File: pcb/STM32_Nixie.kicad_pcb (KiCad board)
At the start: 2 copper layers, 15 parts, among them U1 IC_HV5622PG-G, U2 IC_HV5622PG-G, U3 STM32F100C4Tx

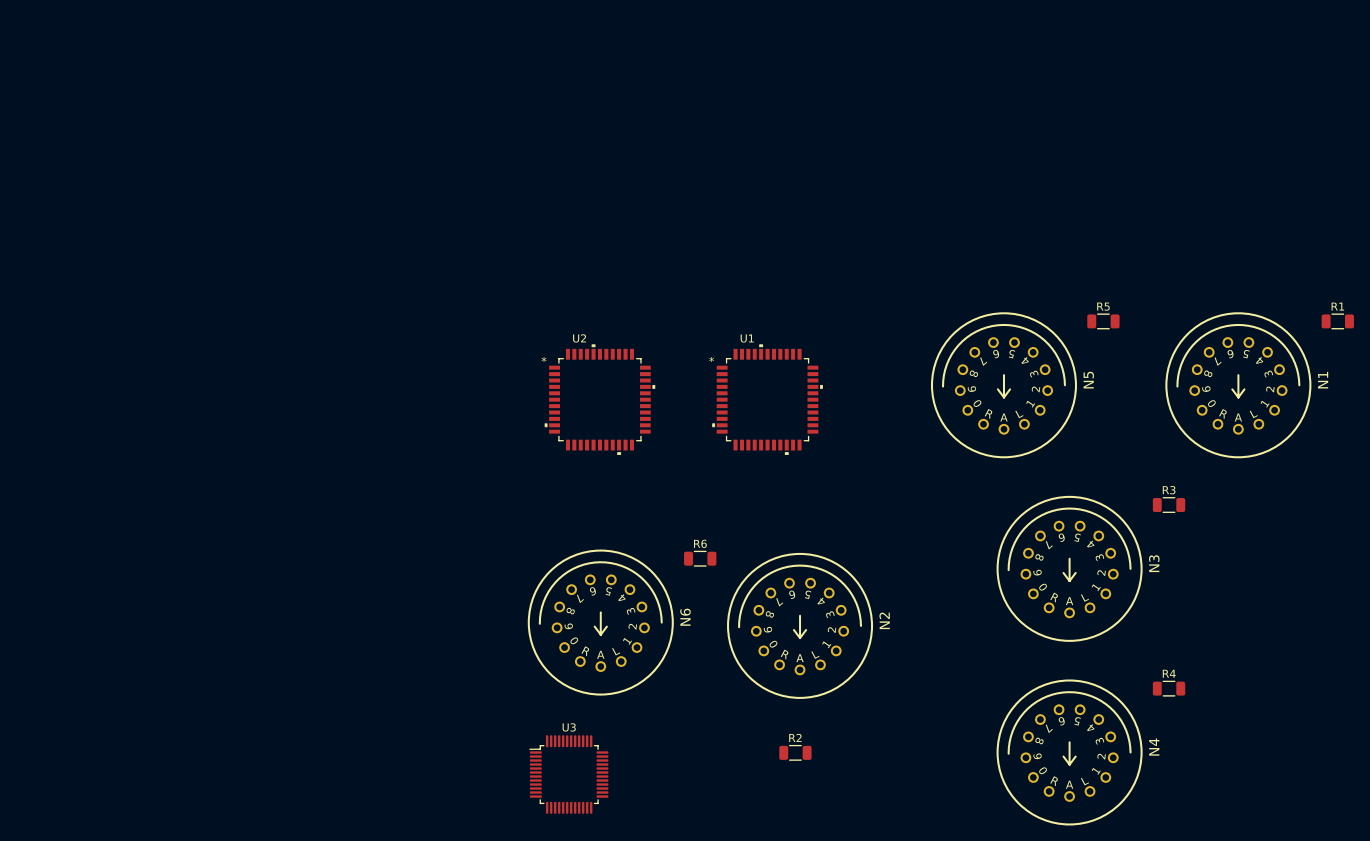
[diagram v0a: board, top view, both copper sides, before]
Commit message: Added ferrite to ADC input, Coin-Cell, and STLINK conn.
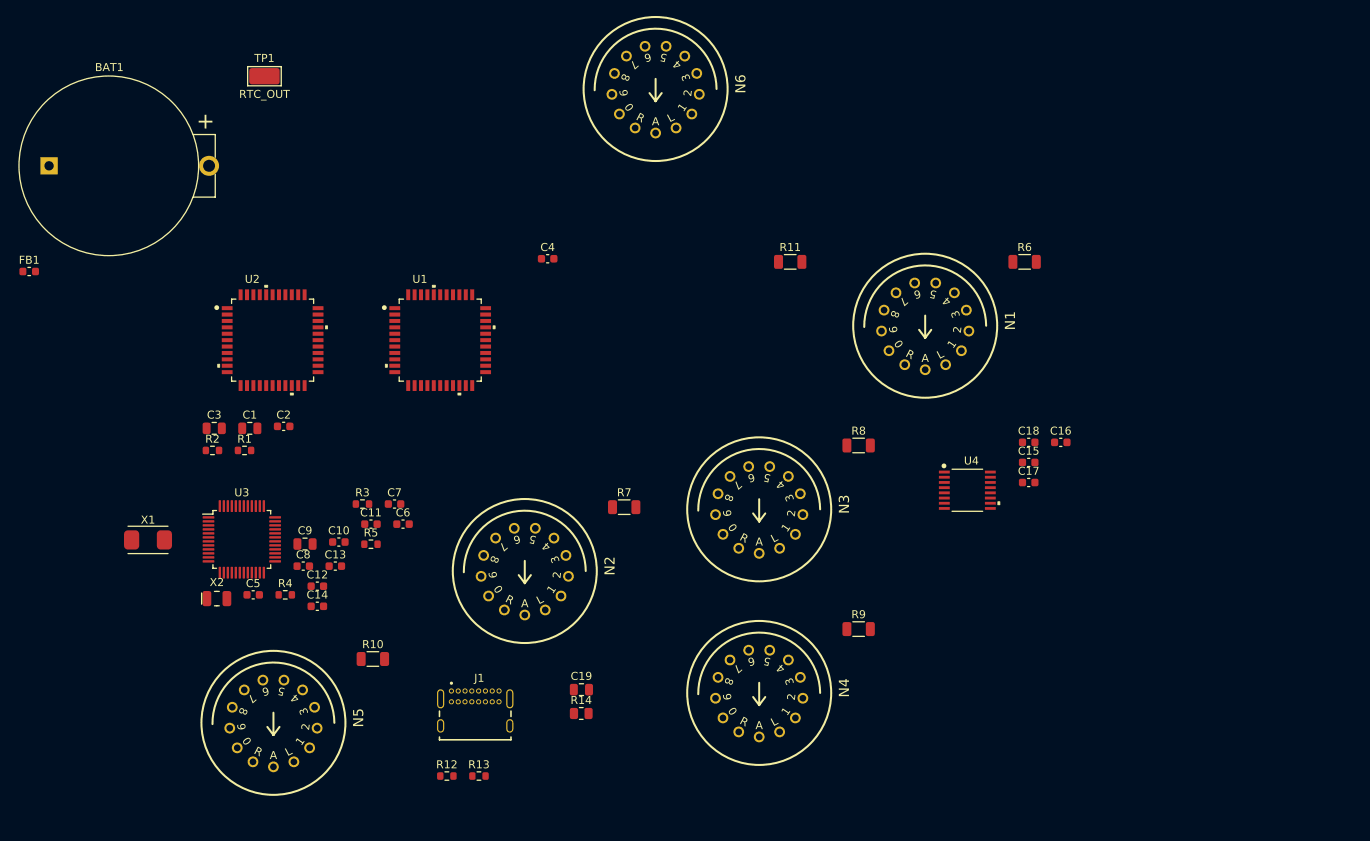
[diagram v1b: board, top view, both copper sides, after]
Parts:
- added BAT1: BS-7, arjun_footprints:Battery_Holder_Coin_2032_BS-7, F.Cu at (110.9, 55.8)
- added C1: CAP_CER_4u7_50V_X5R_0805, Capacitor_SMD:C_0805_2012Metric, F.Cu at (136.0, 88.6)
- added C10: CAP_CER_0u1_50V_X7R_0603, Capacitor_SMD:C_0603_1608Metric, F.Cu at (147.1, 102.8)
- added C11: CAP_CER_0u1_50V_X7R_0603, Capacitor_SMD:C_0603_1608Metric, F.Cu at (151.1, 100.6)
- added C12: CAP_CER_0u1_50V_X7R_0603, Capacitor_SMD:C_0603_1608Metric, F.Cu at (144.4, 108.3)
- added C13: CAP_CER_1u_25V_X5R_0603, Capacitor_SMD:C_0603_1608Metric, F.Cu at (146.7, 105.8)
- added C14: CAP_CER_0u1_50V_X7R_0603, Capacitor_SMD:C_0603_1608Metric, F.Cu at (144.4, 110.8)
- added C15: CAP_CER_1u_25V_X5R_0603, Capacitor_SMD:C_0603_1608Metric, F.Cu at (233.3, 92.9)
- added C16: CAP_CER_0u1_50V_X7R_0603, Capacitor_SMD:C_0603_1608Metric, F.Cu at (237.3, 90.3)
- added C17: CAP_CER_0u1_50V_X7R_0603, Capacitor_SMD:C_0603_1608Metric, F.Cu at (233.3, 95.4)
- added C18: CAP_CER_1u_25V_X5R_0603, Capacitor_SMD:C_0603_1608Metric, F.Cu at (233.3, 90.3)
- added C19: CAP_CER_4700p_250V_X7R_0805, Capacitor_SMD:C_0805_2012Metric, F.Cu at (177.4, 121.3)
- added C2: CAP_CER_0u1_50V_X7R_0603, Capacitor_SMD:C_0603_1608Metric, F.Cu at (140.2, 88.3)
- added C3: CAP_CER_4u7_50V_X5R_0805, Capacitor_SMD:C_0805_2012Metric, F.Cu at (131.5, 88.6)
- added C4: CAP_CER_0u1_50V_X7R_0603, Capacitor_SMD:C_0603_1608Metric, F.Cu at (173.2, 67.4)
- added C5: CAP_CER_27p_50V_NP0_0603, Capacitor_SMD:C_0603_1608Metric, F.Cu at (136.4, 109.4)
- added C6: CAP_CER_27p_50V_NP0_0603, Capacitor_SMD:C_0603_1608Metric, F.Cu at (155.1, 100.6)
- added C7: CAP_CER_8p_50V_NP0_0603, Capacitor_SMD:C_0603_1608Metric, F.Cu at (154.1, 98.1)
- added C8: CAP_CER_8p_50V_NP0_0603, Capacitor_SMD:C_0603_1608Metric, F.Cu at (142.6, 105.8)
- added C9: CAP_CER_10u_16V_X5R_0805, Capacitor_SMD:C_0805_2012Metric, F.Cu at (142.9, 103.1)
- added FB1: FER_1K_600mA_0603, Inductor_SMD:L_0603_1608Metric, F.Cu at (108.4, 69.0)
- added J1: CONN_USBC_RCPT_USB2.0_USB4085-GF-A, arjun_footprints:GCT_USB4085-GF-A_REVA4, F.Cu at (164.1, 125.8)
- added R10: RES_17K4_1P_1/4W_1206, Resistor_SMD:R_1206_3216Metric, F.Cu at (151.3, 117.4)
- added R11: RES_17K4_1P_1/4W_1206, Resistor_SMD:R_1206_3216Metric, F.Cu at (203.5, 67.8)
- added R12: RES_5K11_1P_1/10W_0603, Resistor_SMD:R_0603_1608Metric, F.Cu at (160.6, 132.1)
- added R13: RES_5K11_1P_1/10W_0603, Resistor_SMD:R_0603_1608Metric, F.Cu at (164.6, 132.1)
- added R14: RES_0R_1/8W_0805, Resistor_SMD:R_0805_2012Metric, F.Cu at (177.4, 124.2)
- added R7: RES_17K4_1P_1/4W_1206, Resistor_SMD:R_1206_3216Metric, F.Cu at (182.8, 98.4)
- added R8: RES_17K4_1P_1/4W_1206, Resistor_SMD:R_1206_3216Metric, F.Cu at (212.1, 90.7)
- added R9: RES_17K4_1P_1/4W_1206, Resistor_SMD:R_1206_3216Metric, F.Cu at (212.1, 113.7)
- added TP1: RTC_OUT, arjun_footprints:TestPoint_Keystone_5019_Minature, F.Cu at (137.8, 44.6)
- added U4: IC_LVL_MC14504BDTR2G, arjun_footprints:MC14504BDTR2G, F.Cu at (225.7, 96.3)
- added X1: XTAL_8M_20PPM_18pF_ECS-80-18-30-JGN-TR, arjun_footprints:SMD-2_5x3.2mm_ECS, F.Cu at (123.2, 102.5)
- added X2: XTAL_32K768_10PPM_7pF_ECS-.327-7-34B-C-TR, arjun_footprints:SMD-2_3.2x1.5mm_ECS, F.Cu at (131.8, 109.9)
- R1, R2, R3: value R_17K4_1P_1/4W_1206 -> RES_10K_1P_1/10W_0603; footprint Resistor_SMD:R_1206_3216Metric -> Resistor_SMD:R_0603_1608Metric
- R4: value R_17K4_1P_1/4W_1206 -> RES_732R_1P_1/10W_0603; footprint Resistor_SMD:R_1206_3216Metric -> Resistor_SMD:R_0603_1608Metric
- R5: value R_17K4_1P_1/4W_1206 -> RES_0R_1/10W_0603; footprint Resistor_SMD:R_1206_3216Metric -> Resistor_SMD:R_0603_1608Metric
- R6: value R_17K4_1P_1/4W_1206 -> RES_17K4_1P_1/4W_1206
- U3: value STM32F100C4Tx -> IC_MCU_STM32F100C4T6B_48LQFP
- moved R1 137.6 mm to (135.3, 91.4)
- moved R4 111.1 mm to (140.4, 109.4)
- moved R3 100.8 mm to (150.0, 98.1)
- moved N5 100.6 mm to (138.9, 125.4)
- moved R5 95.7 mm to (151.1, 103.1)
- moved R2 82.1 mm to (131.3, 91.4)
- moved N6 67.0 mm to (186.7, 46.2)
- moved R6 55.0 mm to (232.8, 67.8)
- moved U3 50.4 mm to (135.0, 102.5)
- moved U1 41.6 mm to (159.8, 77.6)
- moved U2 41.6 mm to (138.8, 77.6)
- moved N1 39.9 mm to (220.4, 75.8)
- moved N3 39.5 mm to (199.6, 98.7)
- moved N4 39.5 mm to (199.6, 121.7)
- moved N2 35.1 mm to (170.3, 106.4)
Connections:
- R1 pad 1: 180V -> +12V
- R1 pad 2: /Shift Registers/H1/NIXIE_A -> /Shift Registers/nPOL_12V
- R2 pad 1: 180V -> /PWM_nBL_12V
- R2 pad 2: /Shift Registers/H2/NIXIE_A -> GND
- R3 pad 1: 180V -> +3.3V
- R3 pad 2: /Shift Registers/M1/NIXIE_A -> /MCU/nRST
- R4 pad 1: 180V -> /MCU/OSC_OUT
- R4 pad 2: /Shift Registers/M2/NIXIE_A -> /MCU/OSC_OUT_R
- R5 pad 1: 180V -> /MCU/OSC32_OUT
- R5 pad 2: /Shift Registers/S1/NIXIE_A -> /MCU/OSC32_OUT_R
- R6 pad 2: /Shift Registers/S2/NIXIE_A -> /Shift Registers/H1/NIXIE_A
- U1 pad 23: unconnected-(U1-Pad23) -> /Shift Registers/DATA_CHAIN
- U1 pad 27: unconnected-(U1-Pad27) -> /Shift Registers/nPOL_12V
- U1 pad 28: unconnected-(U1-Pad28) -> /SPI_SCK_12V
- U1 pad 29: unconnected-(U1-Pad29) -> GND
- U1 pad 30: unconnected-(U1-Pad30) -> +12V
- U1 pad 31: unconnected-(U1-Pad31) -> /SPI_nCS_nLE_12V
- U1 pad 32: unconnected-(U1-Pad32) -> /SPI_PICO_12V
- U1 pad 33: unconnected-(U1-Pad33) -> /PWM_nBL_12V
- U2 pad 27: unconnected-(U2-Pad27) -> /PWM_nBL_12V
- U2 pad 28: unconnected-(U2-Pad28) -> /SPI_SCK_12V
- U2 pad 29: unconnected-(U2-Pad29) -> GND
- U2 pad 30: unconnected-(U2-Pad30) -> +12V
- U2 pad 31: unconnected-(U2-Pad31) -> /SPI_nCS_nLE_12V
- U2 pad 32: unconnected-(U2-Pad32) -> /Shift Registers/DATA_CHAIN
- U2 pad 33: unconnected-(U2-Pad33) -> /Shift Registers/nPOL_12V
- U3 pad 1: unconnected-(U3-Pad1) -> 180V
- U3 pad 11: unconnected-(U3-Pad11) -> /MCU/HV_MON_BUF
- U3 pad 12: unconnected-(U3-Pad12) -> /MCU/UART_VCP_TX
- U3 pad 13: unconnected-(U3-Pad13) -> /MCU/UART_VCP_RX
- U3 pad 14: unconnected-(U3-Pad14) -> /SPI_nCS_nLE_3V3
- U3 pad 15: unconnected-(U3-Pad15) -> /SPI_SCK_3V3
- U3 pad 16: unconnected-(U3-Pad16) -> /PWM_nBL_3V3
- U3 pad 17: unconnected-(U3-Pad17) -> /SPI_PICO_3V3
- U3 pad 18: unconnected-(U3-Pad18) -> /nPOL_3V3
- U3 pad 2: unconnected-(U3-Pad2) -> /MCU/RTC_OUT
- U3 pad 23: unconnected-(U3-Pad23) -> GND
- U3 pad 24: unconnected-(U3-Pad24) -> +3.3V
- U3 pad 25: unconnected-(U3-Pad25) -> /MCU/HV_EN
- U3 pad 3: unconnected-(U3-Pad3) -> /MCU/OSC32_IN
- U3 pad 30: unconnected-(U3-Pad30) -> /MCU/UART_BL_TX
- U3 pad 31: unconnected-(U3-Pad31) -> /MCU/UART_BL_RX
- U3 pad 34: unconnected-(U3-Pad34) -> /MCU/SWDIO
- U3 pad 35: unconnected-(U3-Pad35) -> GND
- U3 pad 36: unconnected-(U3-Pad36) -> +3.3V
- U3 pad 37: unconnected-(U3-Pad37) -> /MCU/SWCLK
- U3 pad 39: unconnected-(U3-Pad39) -> /MCU/SWO
- U3 pad 4: unconnected-(U3-Pad4) -> /MCU/OSC32_OUT
- U3 pad 47: unconnected-(U3-Pad47) -> GND
- U3 pad 48: unconnected-(U3-Pad48) -> +3.3V
- U3 pad 5: unconnected-(U3-Pad5) -> /MCU/OSC_IN
- U3 pad 6: unconnected-(U3-Pad6) -> /MCU/OSC_OUT
- U3 pad 7: unconnected-(U3-Pad7) -> /MCU/nRST
- U3 pad 8: unconnected-(U3-Pad8) -> GND
- U3 pad 9: unconnected-(U3-Pad9) -> +3.3VA

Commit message: Added snubber DNP footprints and named nets on power page.
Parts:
- added C10: CAP_CER_0u1_50V_X7R_0603, Capacitor_SMD:C_0603_1608Metric, F.Cu at (92.3, 121.9)
- added C21: CAP_CER_1u_50V_X7R_0805, Capacitor_SMD:C_0805_2012Metric, F.Cu at (16.6, 76.7)
- added C22: CAP_CER_0u1_50V_X7R_0603, Capacitor_SMD:C_0603_1608Metric, F.Cu at (42.1, 128.2)
- added C23: CAP_CER_100u_10V_X5R_1210, Capacitor_SMD:C_1210_3225Metric, F.Cu at (23.4, 132.2)
- added C24: CAP_CER_100u_10V_X5R_1210, Capacitor_SMD:C_1210_3225Metric, F.Cu at (49.3, 111.8)
- added C25: CAP_CER_100u_10V_X5R_1210, Capacitor_SMD:C_1210_3225Metric, F.Cu at (29.0, 132.3)
- added C26: CAP_CER_1u_50V_X7R_0805, Capacitor_SMD:C_0805_2012Metric, F.Cu at (37.9, 128.4)
- added C27: CAP_CER_0u1_50V_X7R_0603, Capacitor_SMD:C_0603_1608Metric, F.Cu at (42.3, 130.7)
- added C28: CAP_CER_0u1_50V_X7R_0603, Capacitor_SMD:C_0603_1608Metric, F.Cu at (49.6, 121.4)
- added C29: CAP_CER_4u7_50V_X7R_1206, Capacitor_SMD:C_1206_3216Metric, F.Cu at (40.4, 118.3)
- added C30: CAP_CER_4u7_50V_X7R_1206, Capacitor_SMD:C_1206_3216Metric, F.Cu at (40.4, 121.7)
- added C31: CAP_CER_0u01_50V_X7R_0603, Capacitor_SMD:C_0603_1608Metric, F.Cu at (47.7, 124.0)
- added C32: CAP_CER_0u1_50V_X7R_0603, Capacitor_SMD:C_0603_1608Metric, F.Cu at (42.3, 133.2)
- added C33: CAP_CER_1u_16V_X7R_0603, Capacitor_SMD:C_0603_1608Metric, F.Cu at (53.7, 121.4)
- added C34: CAP_CER_1500p_50V_NP0_0603, Capacitor_SMD:C_0603_1608Metric, F.Cu at (38.3, 133.7)
- added C35: CAP_CER_3300p_50V_X7R_0603, Capacitor_SMD:C_0603_1608Metric, F.Cu at (46.3, 131.5)
- added C36: CAP_CER_7p_50V_NP0_0603, Capacitor_SMD:C_0603_1608Metric, F.Cu at (46.3, 129.0)
- added C37: CAP_CER_1u_50V_X7R_0805, Capacitor_SMD:C_0805_2012Metric, F.Cu at (45.4, 121.2)
- added C38: CAP_CER_0u1_50V_X7R_0603, Capacitor_SMD:C_0603_1608Metric, F.Cu at (51.7, 126.4)
- added C39: CAP_CER_DNP_0805, Capacitor_SMD:C_0805_2012Metric, F.Cu at (33.2, 83.5)
- added C40: CAP_CER_DNP_0805, Capacitor_SMD:C_0805_2012Metric, F.Cu at (28.3, 83.3)
- added C41: CAP_CER_0u1_50V_X7R_0603, Capacitor_SMD:C_0603_1608Metric, F.Cu at (62.8, 116.0)
- added C42: CAP_CER_1u_50V_X7R_0805, Capacitor_SMD:C_0805_2012Metric, F.Cu at (50.6, 115.7)
- added C43: CAP_CER_0u1_250V_X7R_0805, Capacitor_SMD:C_0805_2012Metric, F.Cu at (34.1, 131.7)
- added C44: CAP_CER_1u_250V_X7R_2220, Capacitor_SMD:C_2220_5650Metric, F.Cu at (33.3, 120.1)
- added C45: CAP_CER_1u_250V_X7R_2220, Capacitor_SMD:C_2220_5650Metric, F.Cu at (24.8, 126.6)
- added C46: CAP_CER_1u_250V_X7R_2220, Capacitor_SMD:C_2220_5650Metric, F.Cu at (33.9, 113.2)
- added C47: CAP_CER_0u1_50V_X7R_0603, Capacitor_SMD:C_0603_1608Metric, F.Cu at (46.5, 143.3)
- added C48: CAP_CER_0u01_50V_X7R_0603, Capacitor_SMD:C_0603_1608Metric, F.Cu at (38.4, 148.3)
- added C49: CAP_CER_0u01_50V_X7R_0603, Capacitor_SMD:C_0603_1608Metric, F.Cu at (38.4, 143.3)
- added C51: CAP_CER_0u01_50V_X7R_0603, Capacitor_SMD:C_0603_1608Metric, F.Cu at (60.6, 154.9)
- added C52: CAP_CER_0u1_50V_X7R_0603, Capacitor_SMD:C_0603_1608Metric, F.Cu at (61.1, 151.9)
- added C53: CAP_CER_4u7_50V_X5R_0805, Capacitor_SMD:C_0805_2012Metric, F.Cu at (56.8, 152.1)
- added C9: CAP_CER_0u1_50V_X7R_0603, Capacitor_SMD:C_0603_1608Metric, F.Cu at (94.0, 119.4)
- added D1: D_300V_2A_SMB, Diode_SMD:D_SMB, F.Cu at (35.6, 88.9)
- added FB1: FER_1K_0A6_0603, Inductor_SMD:L_0603_1608Metric, F.Cu at (88.3, 125.4)
- added FB2: FER_120R_2A_0603, Inductor_SMD:L_0603_1608Metric, F.Cu at (63.3, 111.0)
- added FB3: FER_120R_2A_0603, Inductor_SMD:L_0603_1608Metric, F.Cu at (59.3, 113.5)
- added FB4: FER_120R_2A_0603, Inductor_SMD:L_0603_1608Metric, F.Cu at (58.8, 116.0)
- added FB5: FER_33R_6A_0603, Inductor_SMD:L_0603_1608Metric, F.Cu at (64.6, 154.4)
- added J1: CON_SAMTEC_14P_2R_1m27_P_KEY_FTSH-107-01-L-DV-K-TR, arjun_footprints:CON_FTSH-107-01-x-DV-K, F.Cu at (87.8, 113.9)
- added J2: CONN_USBC_RCPT_USB2.0_USB4085-GF-A, arjun_footprints:GCT_USB4085-GF-A_REVA4, F.Cu at (60.2, 145.6)
- added JP1: SolderJumper_3_Bridged12, Jumper:SolderJumper-3_P1.3mm_Bridged12_RoundedPad1.0x1.5mm_NumberLabels, F.Cu at (85.1, 119.9)
- added L1: IND_22u_1A4_163m8R_4r9x4r9x4, arjun_footprints:IND_Taiyo-Yuden_NR-50xx, F.Cu at (43.2, 104.1)
- added L2: IND_3u3_4A2_35m1R_5x5x4r5, arjun_footprints:IND_VLS5045EX-3R3N, F.Cu at (32.3, 126.9)
- added N1: IN-3, arjun_footprints:IN-3, F.Cu at (86.7, 142.3)
- added N2: IN-3, arjun_footprints:IN-3, F.Cu at (86.7, 134.1)
- added Q1: NFET_250V_10A_TPH1110FNH,L1Q, arjun_footprints:SOP Advance_TOS, F.Cu at (26.4, 89.5)
- added R10: RES_10K_1P_1/10W_0603, Resistor_SMD:R_0603_1608Metric, F.Cu at (88.3, 122.9)
- added R17: RES_10K_1P_1/10W_0603, Resistor_SMD:R_0603_1608Metric, F.Cu at (38.3, 131.2)
- added R18: RES_0R_1/10W_0603, Resistor_SMD:R_0603_1608Metric, F.Cu at (54.8, 115.4)
- added R19: RES_10K_1P_1/10W_0603, Resistor_SMD:R_0603_1608Metric, F.Cu at (63.3, 113.5)
- added R20: RES_10K_1P_1/10W_0603, Resistor_SMD:R_0603_1608Metric, F.Cu at (47.7, 126.5)
- added R23: RES_10K_1P_1/10W_0603, Resistor_SMD:R_0603_1608Metric, F.Cu at (33.8, 134.4)
- added R24: RES_61K9_1P_1/10W_0603, Resistor_SMD:R_0603_1608Metric, F.Cu at (55.7, 123.9)
- added R25: RES_0R_1/10W_0603, Resistor_SMD:R_0603_1608Metric, F.Cu at (58.8, 118.5)
- added R26: RES_0R_1/10W_0603, Resistor_SMD:R_0603_1608Metric, F.Cu at (54.8, 118.4)
- added R27: RES_69K8_1P_1/10W_0603, Resistor_SMD:R_0603_1608Metric, F.Cu at (50.3, 129.0)
- added R28: RES_100R_1P_1/10W_0603, Resistor_SMD:R_0603_1608Metric, F.Cu at (59.3, 111.0)
- added R29: RES_R030_1P_1W_1206, Resistor_SMD:R_1206_3216Metric, F.Cu at (18.3, 87.4)
- added R3: RES_150K_1P_1/4W_1206, Resistor_SMD:R_1206_3216Metric, F.Cu at (94.0, 131.4)
- added R30: RES_DNP_0805, Resistor_SMD:R_0805_2012Metric, F.Cu at (23.9, 83.4)
- added R31: RES_DNP_0805, Resistor_SMD:R_0805_2012Metric, F.Cu at (37.4, 83.5)
- added R32: RES_499K_1P_1/4W_0805, Resistor_SMD:R_0805_2012Metric, F.Cu at (50.5, 118.7)
- added R33: RES_2K8_1P_1/10W_0603, Resistor_SMD:R_0603_1608Metric, F.Cu at (51.7, 123.9)
- added R34: RES_10K_1P_1/10W_0603, Resistor_SMD:R_0603_1608Metric, F.Cu at (42.5, 145.8)
- added R35: RES_10K_1P_1/10W_0603, Resistor_SMD:R_0603_1608Metric, F.Cu at (42.5, 140.8)
- added R36: RES_10K_1P_1/10W_0603, Resistor_SMD:R_0603_1608Metric, F.Cu at (38.4, 145.8)
- added R37: RES_10K_1P_1/10W_0603, Resistor_SMD:R_0603_1608Metric, F.Cu at (42.5, 143.3)
- added R38: RES_10K_1P_1/10W_0603, Resistor_SMD:R_0603_1608Metric, F.Cu at (38.4, 140.8)
- added R39: RES_10K_1P_1/10W_0603, Resistor_SMD:R_0603_1608Metric, F.Cu at (46.5, 140.8)
- added R4: RES_150K_1P_1/4W_1206, Resistor_SMD:R_1206_3216Metric, F.Cu at (94.0, 134.7)
- added R40: RES_0R_1/8W_0805, Resistor_SMD:R_0805_2012Metric, F.Cu at (73.4, 151.4)
- added R41: RES_5K11_1P_1/10W_0603, Resistor_SMD:R_0603_1608Metric, F.Cu at (65.1, 151.9)
- added R42: RES_5K11_1P_1/10W_0603, Resistor_SMD:R_0603_1608Metric, F.Cu at (56.6, 154.9)
- added R5: RES_10K_1P_1/10W_0603, Resistor_SMD:R_0603_1608Metric, F.Cu at (84.3, 125.4)
- added R8: RES_10K_1P_1/10W_0603, Resistor_SMD:R_0603_1608Metric, F.Cu at (84.3, 122.9)
- added R9: RES_10K_1P_1/10W_0603, Resistor_SMD:R_0603_1608Metric, F.Cu at (90.0, 119.4)
- added S1: SW_TACT_PTS645SM43SMTR92_LFS, arjun_footprints:Switch_Tactile_SMD_6x6mm_PTS645, F.Cu at (76.8, 121.0)
- added S2: SW_TACT_PTS645SM43SMTR92_LFS, arjun_footprints:Switch_Tactile_SMD_6x6mm_PTS645, F.Cu at (76.8, 113.5)
- added SW1: ENC_SPST_24PPR_PEC12R-4225F-S0024, arjun_footprints:ENC_SPST_PEC12R-4x25F-Sxxx, F.Cu at (22.8, 148.3)
- added U5: REG_SW_BOOST_TI_TLV61046ADBV, arjun_footprints:SOT-23-6_TI, F.Cu at (45.8, 117.5)
- added U6: REG_SW_BOOST_TI_LM51561HPWPR, arjun_footprints:PWP0014H-MFG, F.Cu at (20.3, 96.5)
- added U7: REG_LDO_3V3_250mA_TI_LP5907MFX-3.3, arjun_footprints:SOT-23-5_TI, F.Cu at (54.7, 111.9)
- added U8: IC_FTDI_FT231XS, Package_SO:SSOP-20_3.9x8.7mm_P0.635mm, F.Cu at (75.2, 144.7)
- U3: footprint Package_QFP:LQFP-48_7x7mm_P0.5mm -> arjun_footprints:LQFP-48_7x7mm_P0.5mm
- renumbered C9 to C11, C10 to C12, C11 to C13, C12 to C14, C13 to C15, C14 to C16, C15 to C17, C16 to C18, C17 to C19, C3 to C2, C18 to C20, C2 to C3, C7 to C6, C6 to C7, N1 to N3, N2 to N4, N3 to N5, N4 to N6, N5 to N7, N6 to N8, R6 to R11, R7 to R12, R8 to R13, R9 to R14, R10 to R15, R11 to R16, R4 to R6, R5 to R7
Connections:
- net /Shift Registers/DATA_CHAIN renamed /Nixie Display/DATA_CHAIN
- net /Shift Registers/H1/NIXIE_A renamed /Nixie Display/H1/NIXIE_A
- net /Shift Registers/H1_0 renamed /Nixie Display/H1_0
- net /Shift Registers/H1_1 renamed /Nixie Display/H1_1
- net /Shift Registers/H1_2 renamed /Nixie Display/H1_2
- net /Shift Registers/H1_3 renamed /Nixie Display/H1_3
- net /Shift Registers/H1_4 renamed /Nixie Display/H1_4
- net /Shift Registers/H1_5 renamed /Nixie Display/H1_5
- net /Shift Registers/H1_6 renamed /Nixie Display/H1_6
- net /Shift Registers/H1_7 renamed /Nixie Display/H1_7
- net /Shift Registers/H1_8 renamed /Nixie Display/H1_8
- net /Shift Registers/H1_9 renamed /Nixie Display/H1_9
- net /Shift Registers/H2/NIXIE_A renamed /Nixie Display/H2/NIXIE_A
- net /Shift Registers/H2_0 renamed /Nixie Display/H2_0
- net /Shift Registers/H2_1 renamed /Nixie Display/H2_1
- net /Shift Registers/H2_2 renamed /Nixie Display/H2_2
- net /Shift Registers/H2_3 renamed /Nixie Display/H2_3
- net /Shift Registers/H2_4 renamed /Nixie Display/H2_4
- net /Shift Registers/H2_5 renamed /Nixie Display/H2_5
- net /Shift Registers/H2_6 renamed /Nixie Display/H2_6
- net /Shift Registers/H2_7 renamed /Nixie Display/H2_7
- net /Shift Registers/H2_8 renamed /Nixie Display/H2_8
- net /Shift Registers/H2_9 renamed /Nixie Display/H2_9
- net /Shift Registers/M1/NIXIE_A renamed /Nixie Display/M1/NIXIE_A
- net /Shift Registers/M1_0 renamed /Nixie Display/M1_0
- net /Shift Registers/M1_1 renamed /Nixie Display/M1_1
- net /Shift Registers/M1_2 renamed /Nixie Display/M1_2
- net /Shift Registers/M1_3 renamed /Nixie Display/M1_3
- net /Shift Registers/M1_4 renamed /Nixie Display/M1_4
- net /Shift Registers/M1_5 renamed /Nixie Display/M1_5
- net /Shift Registers/M1_6 renamed /Nixie Display/M1_6
- net /Shift Registers/M1_7 renamed /Nixie Display/M1_7
- net /Shift Registers/M1_8 renamed /Nixie Display/M1_8
- net /Shift Registers/M1_9 renamed /Nixie Display/M1_9
- net /Shift Registers/M2/NIXIE_A renamed /Nixie Display/M2/NIXIE_A
- net /Shift Registers/M2_0 renamed /Nixie Display/M2_0
- net /Shift Registers/M2_1 renamed /Nixie Display/M2_1
- net /Shift Registers/M2_2 renamed /Nixie Display/M2_2
- net /Shift Registers/M2_3 renamed /Nixie Display/M2_3
- net /Shift Registers/M2_4 renamed /Nixie Display/M2_4
- net /Shift Registers/M2_5 renamed /Nixie Display/M2_5
- net /Shift Registers/M2_6 renamed /Nixie Display/M2_6
- net /Shift Registers/M2_7 renamed /Nixie Display/M2_7
- net /Shift Registers/M2_8 renamed /Nixie Display/M2_8
- net /Shift Registers/M2_9 renamed /Nixie Display/M2_9
- net /Shift Registers/S1/NIXIE_A renamed /Nixie Display/S1/NIXIE_A
- net /Shift Registers/S1_0 renamed /Nixie Display/S1_0
- net /Shift Registers/S1_1 renamed /Nixie Display/S1_1
- net /Shift Registers/S1_2 renamed /Nixie Display/S1_2
- net /Shift Registers/S1_3 renamed /Nixie Display/S1_3
- net /Shift Registers/S1_4 renamed /Nixie Display/S1_4
- net /Shift Registers/S1_5 renamed /Nixie Display/S1_5
- net /Shift Registers/S1_6 renamed /Nixie Display/S1_6
- net /Shift Registers/S1_7 renamed /Nixie Display/S1_7
- net /Shift Registers/S1_8 renamed /Nixie Display/S1_8
- net /Shift Registers/S1_9 renamed /Nixie Display/S1_9
- net /Shift Registers/S2/NIXIE_A renamed /Nixie Display/S2/NIXIE_A
- net /Shift Registers/S2_0 renamed /Nixie Display/S2_0
- net /Shift Registers/S2_1 renamed /Nixie Display/S2_1
- net /Shift Registers/S2_2 renamed /Nixie Display/S2_2
- net /Shift Registers/S2_3 renamed /Nixie Display/S2_3
- net /Shift Registers/S2_4 renamed /Nixie Display/S2_4
- net /Shift Registers/S2_5 renamed /Nixie Display/S2_5
- net /Shift Registers/S2_6 renamed /Nixie Display/S2_6
- net /Shift Registers/S2_7 renamed /Nixie Display/S2_7
- net /Shift Registers/S2_8 renamed /Nixie Display/S2_8
- net /Shift Registers/S2_9 renamed /Nixie Display/S2_9
- net /Shift Registers/nPOL_12V renamed /Nixie Display/nPOL_12V
- U2 pad 37: /Shift Registers/DOT2 -> /Nixie Display/DOT2
- U2 pad 38: /Shift Registers/DOT1 -> /Nixie Display/DOT1
- U3 pad 10: unconnected-(U3-Pad10) -> /MCU/ENC_A_R
- U3 pad 11: /MCU/HV_MON_BUF -> /MCU/ENC_B_R
- U3 pad 18: /nPOL_3V3 -> unconnected-(U3-Pad18)
- U3 pad 19: unconnected-(U3-Pad19) -> /MCU/HV_MON_BUF
- U3 pad 20: unconnected-(U3-Pad20) -> /MCU/BOOT1
- U3 pad 26: unconnected-(U3-Pad26) -> /MCU/nENC_PB_R
- U3 pad 27: unconnected-(U3-Pad27) -> /nPOL_3V3
- U3 pad 44: unconnected-(U3-Pad44) -> /MCU/BOOT0
